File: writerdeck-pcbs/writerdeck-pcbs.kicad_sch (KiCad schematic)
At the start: 0 parts

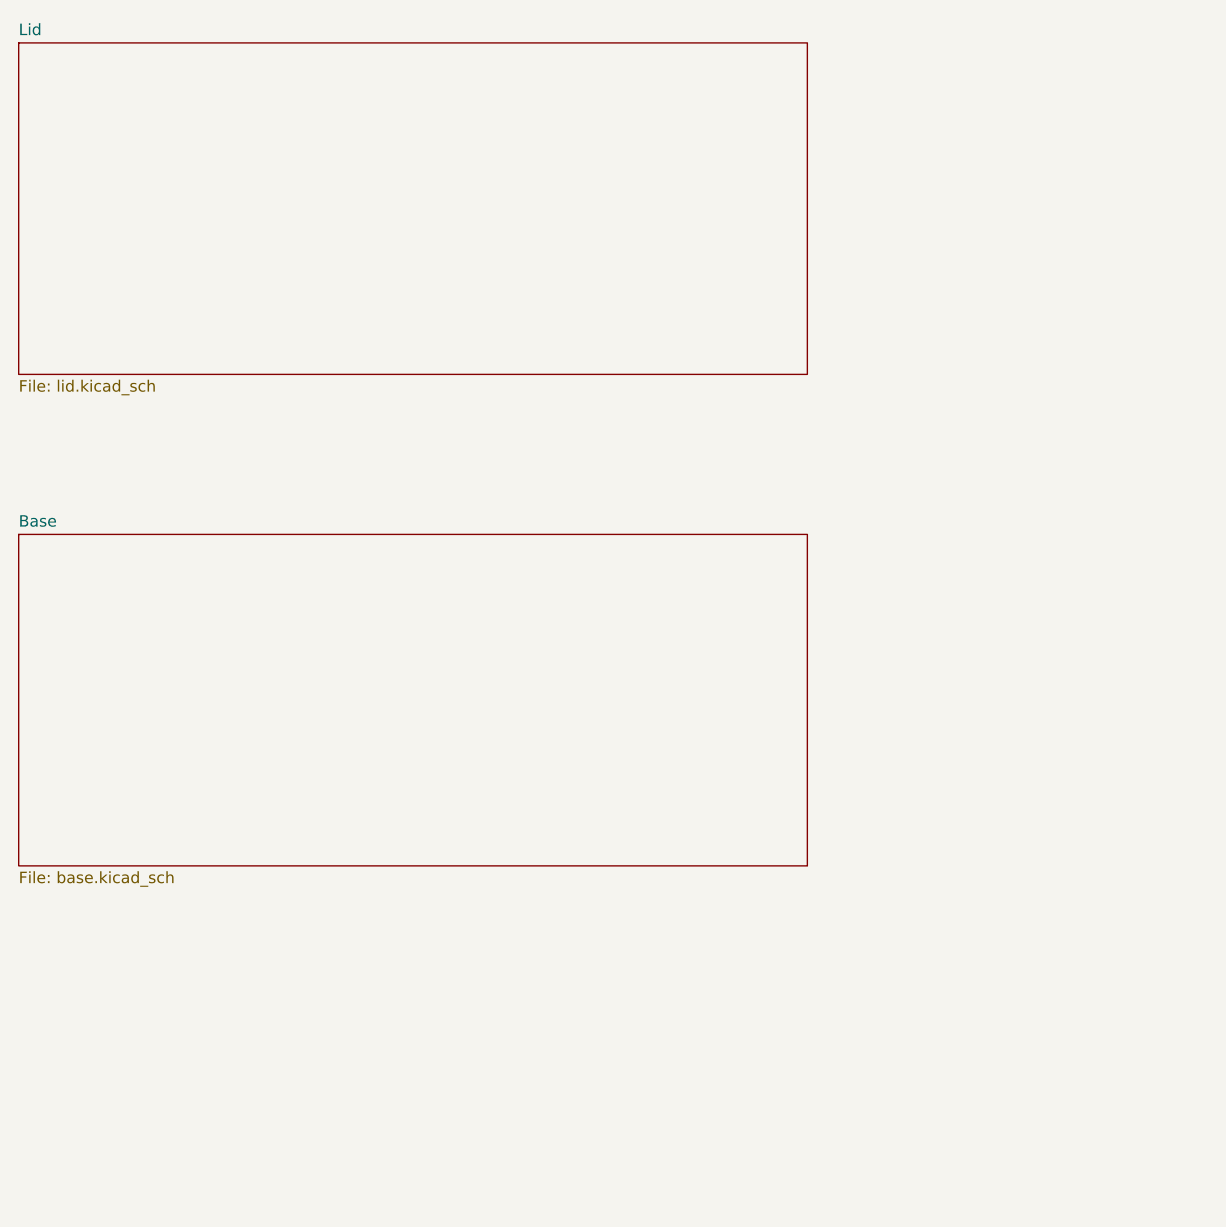
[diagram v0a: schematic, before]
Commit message: pre switch matrix, restructure
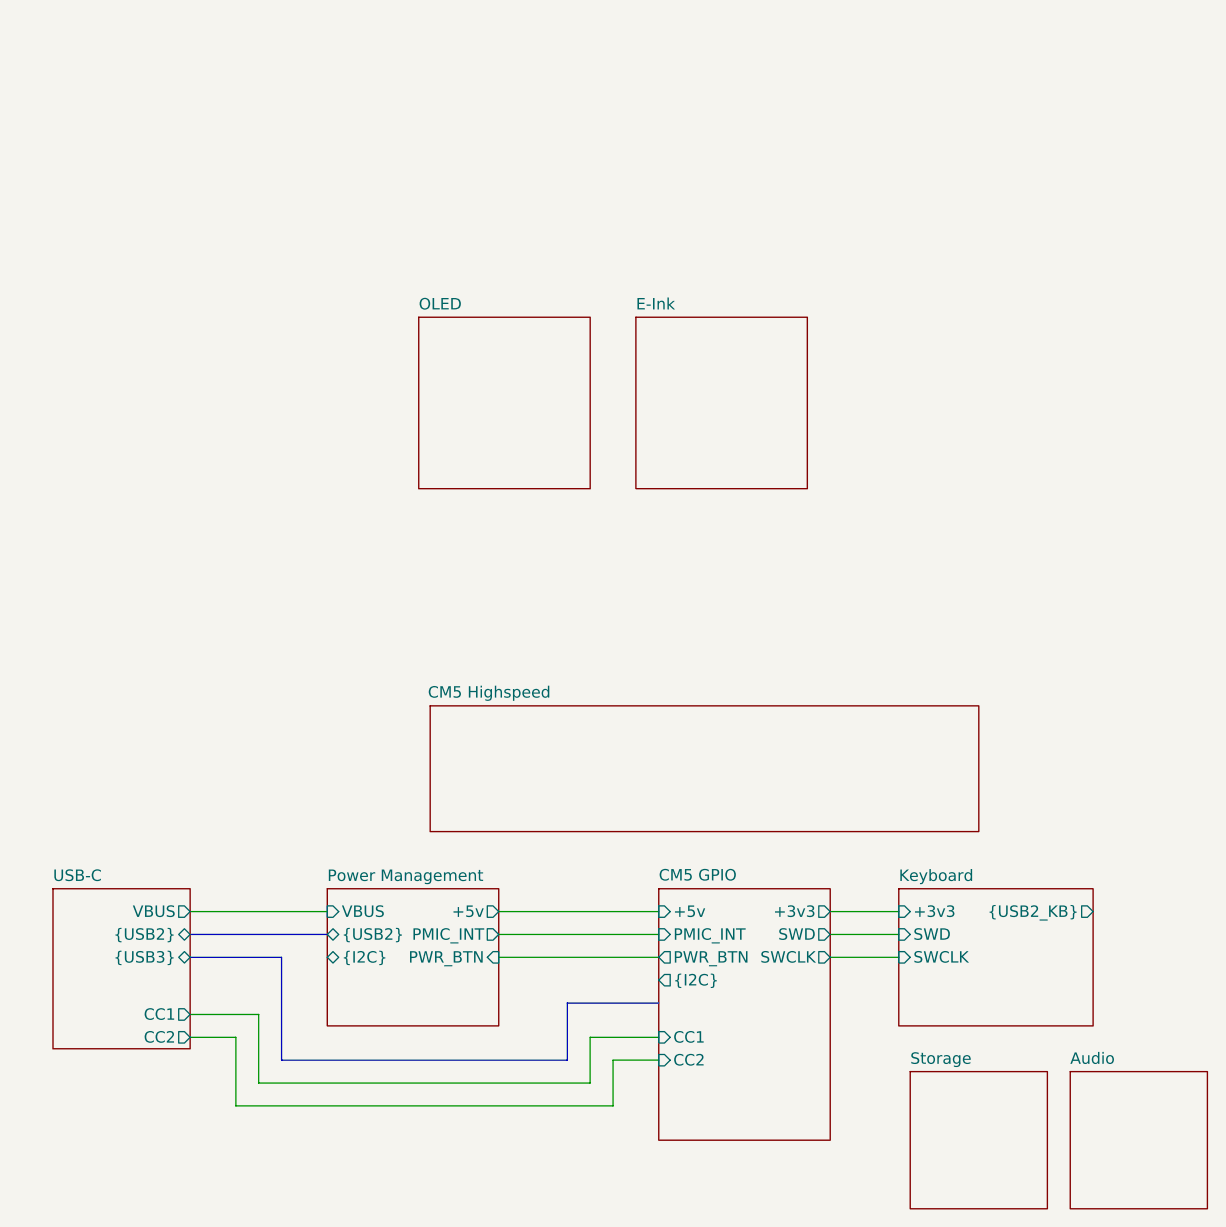
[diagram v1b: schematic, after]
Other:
- removed sheet Base
- removed sheet Lid
- added sheet Audio (audio.kicad_sch)
- added sheet CM5 GPIO (cm5_gpio.kicad_sch)
- added sheet CM5 Highspeed (cm5_highspeed.kicad_sch)
- added sheet E-Ink (e-ink.kicad_sch)
- added sheet Keyboard (HID.kicad_sch)
- added sheet OLED (oled.kicad_sch)
- added sheet Power Management (power-management.kicad_sch)
- added sheet Storage (storage.kicad_sch)
- added sheet USB-C (USB-C.kicad_sch)

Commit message: backup
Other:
- sheet CM5 Highspeed ports: added {USB2}, {USB3}; removed none
- sheet Keyboard ports: added {KB_USB2}; removed {USB2_KB}
